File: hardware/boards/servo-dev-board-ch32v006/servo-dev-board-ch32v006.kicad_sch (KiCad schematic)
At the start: 0 parts

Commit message: copy pasted sg90 prd ch32v006 schematics, and modify to fit. PCB should be about 85x65mm to accomodate TP ring rails for easy hardware testing.
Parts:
- added C1, C8: 10µF, Capacitor_SMD:C_0603_1608Metric, symbol Device:C
- added C2, C3: 1µF, Capacitor_SMD:C_0402_1005Metric, symbol Device:C
- added C4, C5, C6, C7, C9: 0.1µF, Capacitor_SMD:C_0402_1005Metric, symbol Device:C
- added D1: ESD, Diode_SMD:D_SOD-882, symbol Diode:PESD5V0L1UL
- added FB1: 600Ω@100MHz, Inductor_SMD:L_0603_1608Metric, symbol Device:FerriteBead_Small
- added J1: Servo Input, shared:Servo_Output_Pads, symbol Connector_Generic:Conn_01x03
- added J2: Motor, shared:Motor_Wire_Pads, symbol Connector_Generic:Conn_01x02
- added J3: Debug, shared:Debug_Pads_1x4_P1.27mm, symbol Connector_Generic:Conn_01x04
- added J4: Potentiometer, shared:Pot_Wire_Pads, symbol Connector_Generic:Conn_01x03
- added NT2: NetTie_2, shared:NetTie-2_SMD_0.2mm, symbol Device:NetTie_2
- added Q1: AO3401A, Package_TO_SOT_SMD:SOT-23, symbol Transistor_FET:AO3401A
- added R1: 47kΩ, Resistor_SMD:R_0402_1005Metric, symbol Device:R
- added R10, R12, R3, R5, R6: 10kΩ, Resistor_SMD:R_0402_1005Metric, symbol Device:R
- added R11, R9: 20kΩ, Resistor_SMD:R_0402_1005Metric, symbol Device:R
- added R13: 68Ω, Resistor_SMD:R_0402_1005Metric, symbol Device:R
- added R2: 4.7kΩ, Resistor_SMD:R_0402_1005Metric, symbol Device:R
- added R4: 0.1Ω 1%, Resistor_SMD:R_1206_3216Metric, symbol Device:R
- added TH1: NTC 10k, Resistor_SMD:R_0402_1005Metric, symbol Device:Thermistor
- added TP1: TestPoint_Probe, TestPoint:TestPoint_Keystone_5015_Micro_Mini, symbol Connector:TestPoint_Probe
- added U1: TPAP2210K-3.3TRG1, shared:SOT-23-5_L2.9-W1.6-P0.95-LS2.8-BR, symbol shared:TPAP2210K-3.3TRG1
- added U2: 74LVC2G125RA3-7, shared:X2-DFN1210-8_L1.2-W1.0-P0.30-BL, symbol shared:74LVC2G125RA3-7
- added U3: DRV8837DSGR-JSM, Package_SON:WSON-8-1EP_2x2mm_P0.5mm_EP0.9x1.6mm, symbol Driver_Motor:DRV8837C
- added U4: CH32V006F8U6, shared:UQFN-20_L3.0-W3.0-P0.40-BL-EP1.7, symbol shared:CH32V006F8U6
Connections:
- new net +3.3V: C3.1, C4.1, C9.1, FB1.1, J3.1 (Pin_1), J4.1 (Pin_1), R1.2, R5.1, R6.1, U1.5 (VOUT), U2.8 (VCC), U4.6 (VDD)
- new net 3V3_DRV: C6.1, FB1.2, U3.8 (VCC)
- new net BUF: R13.1, U2.5 (2A), U2.6 (1Y)
- new net DATA: D1.1 (K), J1.3 (Pin_3), R13.2
- new net DBG: TP1.1, U4.9 (PC2/T1C3N_/T2/SCL)
- new net DE: U2.7 (~{2OE}), U4.5 (PD0/T1/TX_/SDA_/OPN1)
- new net EN: R3.1, U3.7 (~{SLEEP}), U4.12 (PC5/T1C2_/T1/T2/TX_/SCK)
- new net ENC_A: U4.19 (PD5/T2/TX/RX_/MISO_/A5)
- new net ENC_B: U4.20 (PD6/T2/RX/TX_/MOSI_/A6)
- new net GND: C1.2, C2.2, C3.2, C4.2, C5.2, C9.2, D1.2 (A), J1.1 (Pin_1), J3.2 (Pin_2), J4.3 (Pin_3), Q1.1 (G), R10.2, R12.2, R4.1, TH1.2, U1.2 (GND), U2.2 (1A), U2.4 (GND), U4.21 (VSS), U4.4 (VSS)
- new net IN1: U3.6 (IN1), U4.13 (PC6/T1C3_/T1/RX_/MOSI)
- new net IN2: U3.5 (IN2), U4.14 (PC7/T1C4_/T1/T2/MISO)
- new net ISNS: NT2.1
- new net ISNS+: U4.3 (PA2/T1/T2/U2TX_/OPP0/XO/A0)
- new net ISNS-: U4.2 (PA1/T1/T2/OPN0/XI/A1)
- new net LED: U4.10 (PC3/T1/T2)
- new net OUTA: J2.1 (Pin_1), R9.1, U3.2 (OUT1)
- new net OUTB: J2.2 (Pin_2), R11.1, U3.3 (OUT2)
- new net PGND: C6.2, C7.2, C8.2, NT2.2, R3.2, R4.2, U3.4 (GND), U3.9 (GND)
- new net POT: J4.2 (Pin_2), R2.1
- new net RX: U2.3 (2Y), U4.8 (PC1/T1C2N_/T2/RX_/SDA/NSS)
- new net SWDIO: J3.3 (Pin_3), U4.15 (PD1/SWIO/T1/SCL_/RX_/OPP3)
- new net TX: R1.1, U2.1 (~{1OE}), U4.7 (PC0/T1C1N_/T1/T2/TX_/MOSI_)
- new net VIN: J1.2 (Pin_2), Q1.2 (S)
- new net VNTC: R5.2, TH1.1, U4.18 (PD4/T1/T2/SCK_/OPO0/A7)
- new net VPOS: C5.1, R2.2, U4.16 (PD2/T1/T2/U2TX_/A3)
- new net VSNA: R10.1, R9.2, U4.11 (PC4/T1C1_/T1/MCO/A2)
- new net VSNB: R11.2, R12.1, U4.17 (PD3/T1/T2/U2RX_/NSS_/OPP2/A4)
- new net VSYS: C1.1, C2.1, C7.1, C8.1, Q1.3 (D), U1.1 (VIN), U1.3 (EN), U3.1 (VM)
- new net nRST: J3.4 (Pin_4), R6.2, U4.1 (PD7/RST/T2C4/OPP1/PA4/U2TX_/OPN2)
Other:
- note added: "BEMF SENSE"
- note added: "COMMUNICATION"
- note added: "CONNECTORS"
- note added: "CURRENT SENSE"
- note added: "MCU"
- note added: "MOTOR DRIVER"
- note added: "POSITION SENSOR FILTERING"
- note added: "POWER"
- note added: "TEMP SENSE"

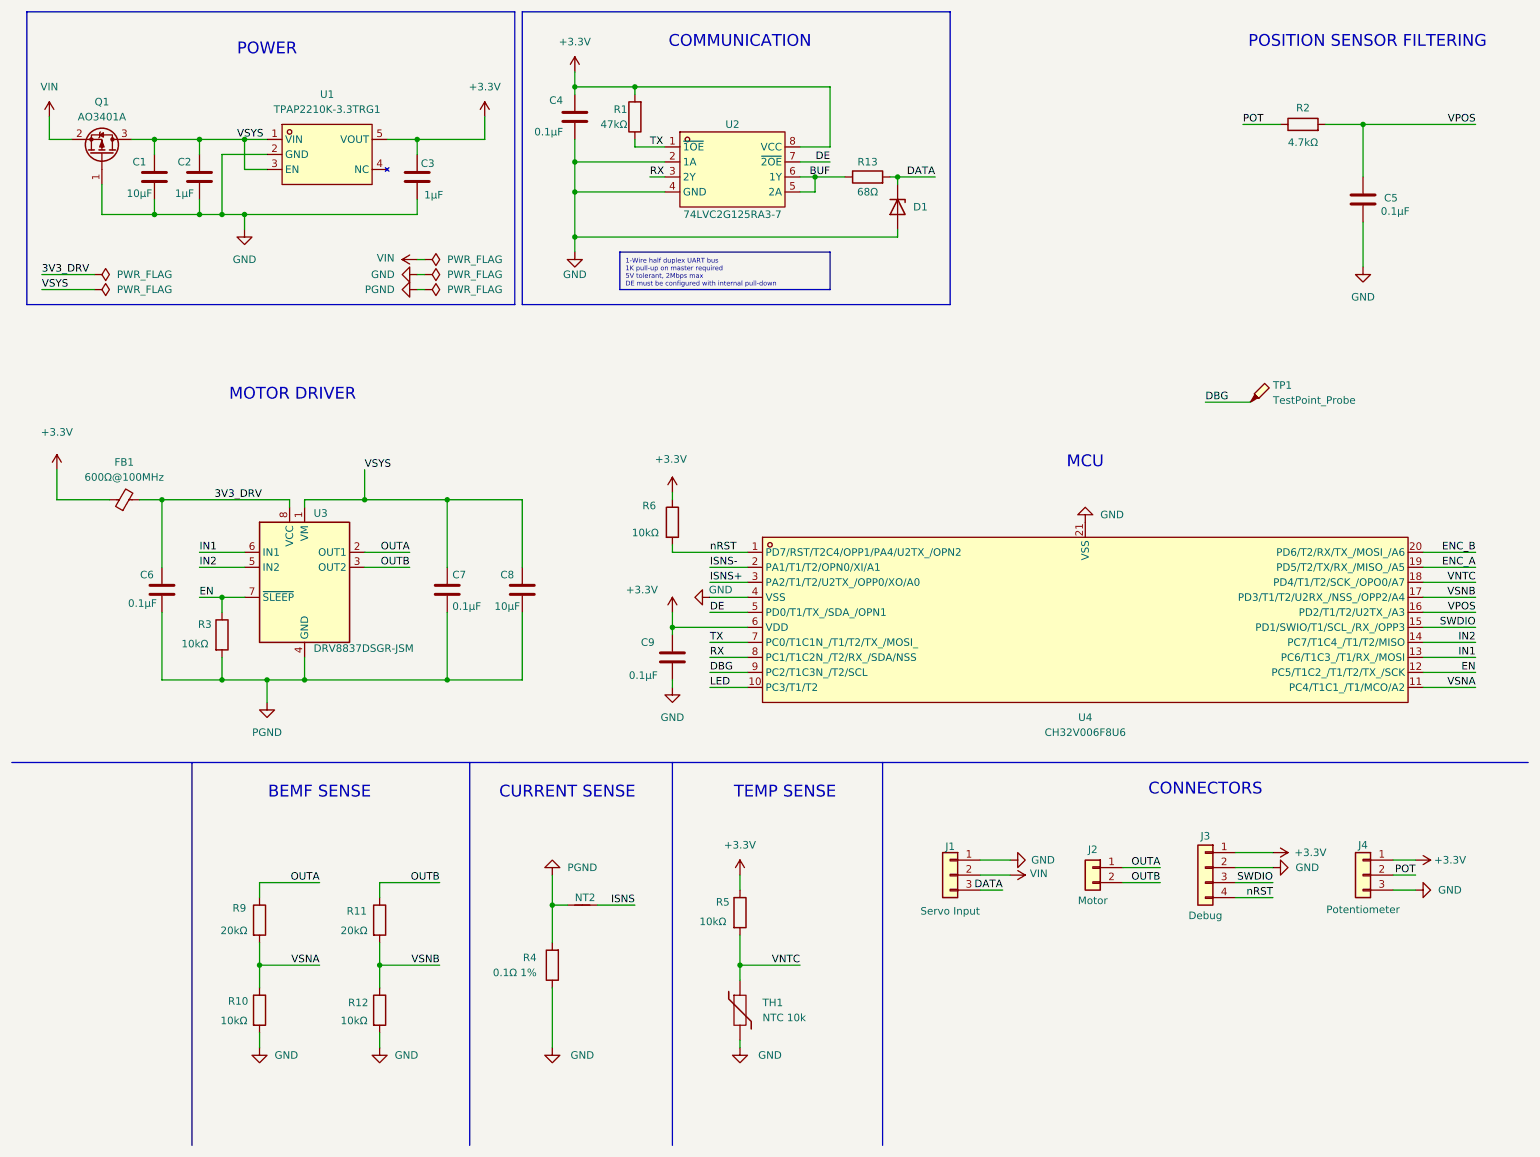
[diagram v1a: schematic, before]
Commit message: mostly done with ch32v006 based dev board schematics. Next is to pick footprint / parts and proceed to PCB design
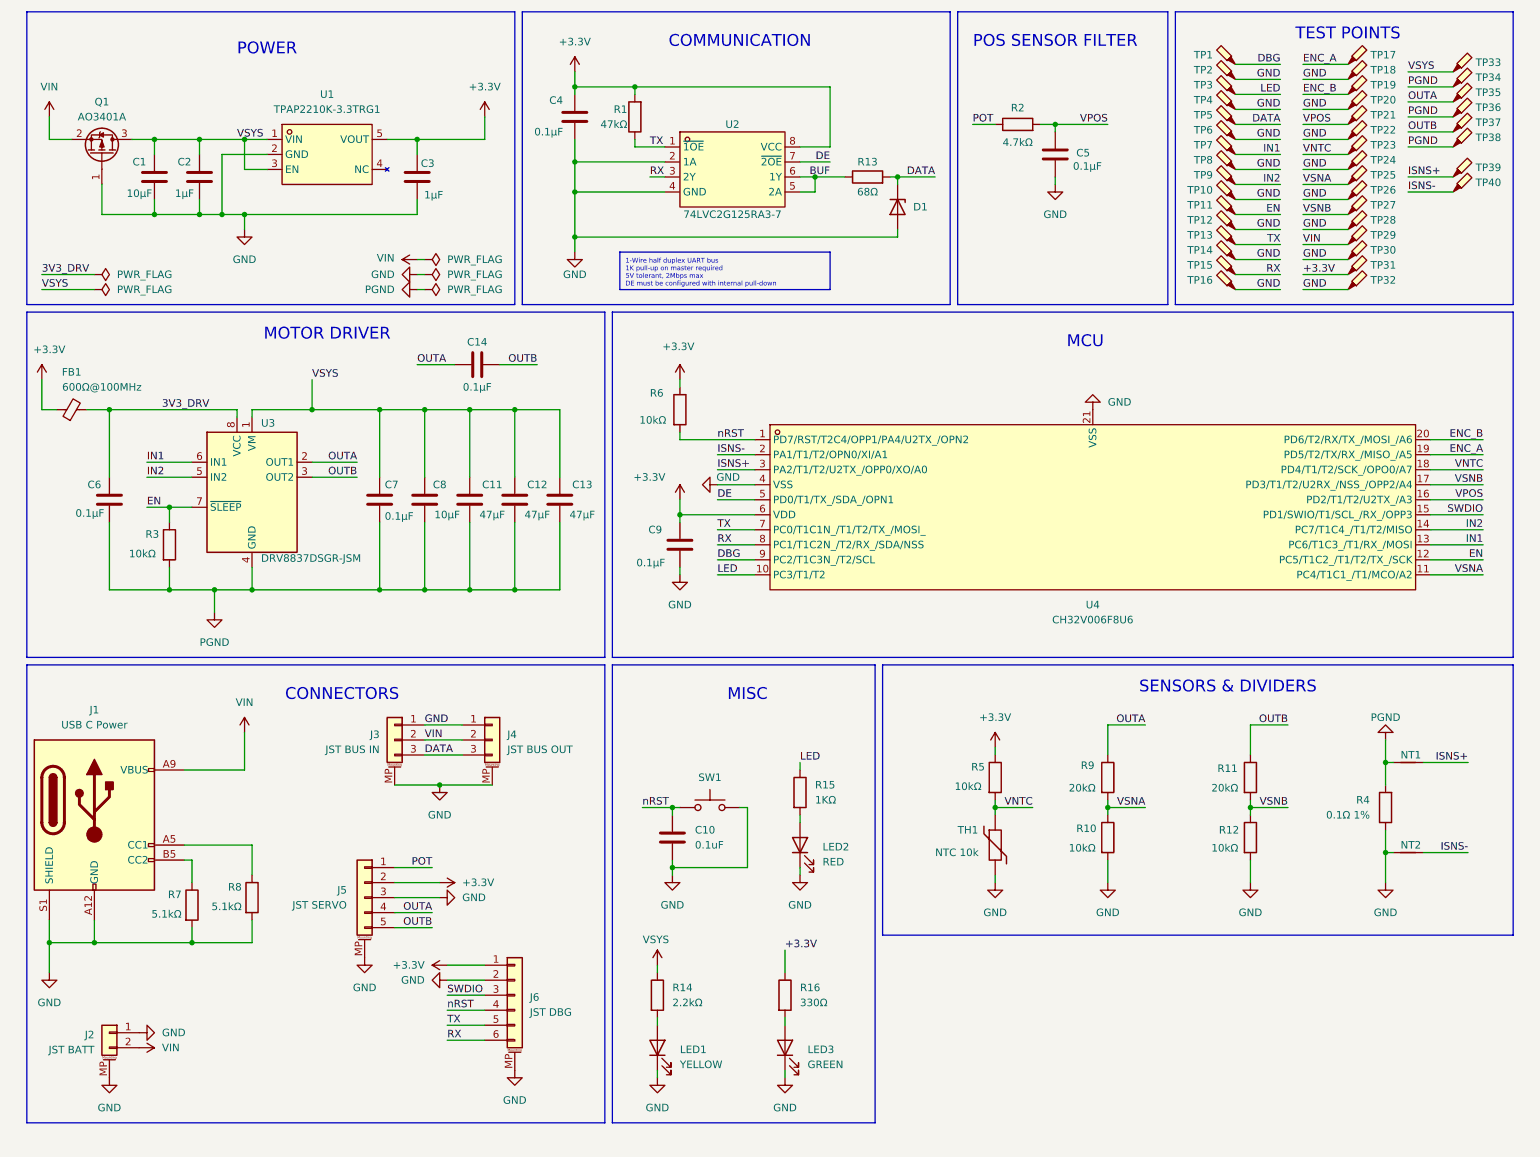
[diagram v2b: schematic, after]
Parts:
- removed J1: Servo Input, shared:Servo_Output_Pads, symbol Connector_Generic:Conn_01x03
- removed J2: Motor, shared:Motor_Wire_Pads, symbol Connector_Generic:Conn_01x02
- removed J3: Debug, shared:Debug_Pads_1x4_P1.27mm, symbol Connector_Generic:Conn_01x04
- removed J4: Potentiometer, shared:Pot_Wire_Pads, symbol Connector_Generic:Conn_01x03
- added C10: 0.1uF, Capacitor_SMD:C_0402_1005Metric, symbol Device:C
- added C11, C12, C13: 47µF, Capacitor_SMD:C_1206_3216Metric, symbol Device:C
- added C14: 0.1µF, Capacitor_SMD:C_0402_1005Metric, symbol Device:C
- added J1: USB C Power, symbol Connector:USB_C_Receptacle_PowerOnly_6P
- added J2: JST BATT, symbol Connector_Generic_MountingPin:Conn_01x02_MountingPin
- added J3: JST BUS IN, symbol Connector_Generic_MountingPin:Conn_01x03_MountingPin
- added J4: JST BUS OUT, symbol Connector_Generic_MountingPin:Conn_01x03_MountingPin
- added J5: JST SERVO, symbol Connector_Generic_MountingPin:Conn_01x05_MountingPin
- added J6: JST DBG, symbol Connector_Generic_MountingPin:Conn_01x06_MountingPin
- added LED1: YELLOW, LED_SMD:LED_0805_2012Metric, symbol Device:LED
- added LED2: RED, LED_SMD:LED_0805_2012Metric, symbol Device:LED
- added LED3: GREEN, LED_SMD:LED_0805_2012Metric, symbol Device:LED
- added NT2: NetTie_2, shared:NetTie-2_SMD_0.2mm, symbol Device:NetTie_2
- added R14: 2.2kΩ, Resistor_SMD:R_0402_1005Metric, symbol Device:R
- added R15: 1KΩ, Resistor_SMD:R_0402_1005Metric, symbol Device:R
- added R16: 330Ω, Resistor_SMD:R_0402_1005Metric, symbol Device:R
- added R7, R8: 5.1kΩ, Resistor_SMD:R_0402_1005Metric, symbol Device:R
- added SW1: SW_Push, Button_Switch_SMD:SW_SPST_PTS810, symbol Switch:SW_Push
- added TP10, TP11, TP12, TP13, TP14, TP15, TP16, TP17, TP18, TP19, TP2, TP20, TP21, TP22, TP23, TP24, TP25, TP26, TP27, TP28, TP29, TP3, TP30, TP31, TP32, TP33, TP34, TP35, TP36, TP37, TP38, TP39, TP4, TP40, TP5, TP6, TP7, TP8, TP9: TestPoint_Probe, TestPoint:TestPoint_Keystone_5015_Micro_Mini, symbol Connector:TestPoint_Probe
- renumbered NT2 to NT1
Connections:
- net ISNS is gone; now on net ISNS+: NT1.1
- net +3.3V: now also J5.2 (Pin_2), J6.1 (Pin_1), R16.1, TP31.1
- net DATA: now also J3.3 (Pin_3), J4.3 (Pin_3), TP5.1
- net EN: now also TP11.1
- net ENC_A: now also TP17.1
- net ENC_B: now also TP19.1
- net GND: now also C10.1, J1.A12 (GND), J1.B12 (GND), J1.S1 (SHIELD), J2.1 (Pin_1), J2.MP (MountPin), J3.1 (Pin_1), J3.MP (MountPin), J4.1 (Pin_1), J4.MP (MountPin), J5.3 (Pin_3), J5.MP (MountPin), J6.2 (Pin_2), J6.MP (MountPin), LED1.1 (K), LED2.1 (K), LED3.1 (K), NT2.2, R7.2, R8.2, SW1.2, TP10.1, TP12.1, TP14.1, TP16.1, TP18.1, TP2.1, TP20.1, TP22.1, TP24.1, TP26.1, TP28.1, TP30.1, TP32.1, TP4.1, TP6.1, TP8.1
- net IN1: now also TP7.1
- net IN2: now also TP9.1
- net ISNS+: now also TP39.1
- net ISNS-: now also NT2.1, TP40.1
- net LED: now also R15.1, TP3.1
- net OUTA: now also C14.1, J5.4 (Pin_4), TP35.1
- net OUTB: now also C14.2, J5.5 (Pin_5), TP37.1
- net PGND: now also C11.2, C12.2, C13.2, TP34.1, TP36.1, TP38.1
- net POT: now also J5.1 (Pin_1)
- net RX: now also J6.6 (Pin_6), TP15.1
- net SWDIO: now also J6.3 (Pin_3)
- net TX: now also J6.5 (Pin_5), TP13.1
- net VIN: now also J1.A9 (VBUS), J1.B9 (VBUS), J2.2 (Pin_2), J3.2 (Pin_2), J4.2 (Pin_2), TP29.1
- net VNTC: now also TP23.1
- net VPOS: now also TP21.1
- net VSNA: now also TP25.1
- net VSNB: now also TP27.1
- net VSYS: now also C11.1, C12.1, C13.1, R14.1, TP33.1
- net nRST: now also C10.2, J6.4 (Pin_4), SW1.1
- new net: LED1.2 (A), R14.2
- new net: LED2.2 (A), R15.2
- new net: J1.A5 (CC1), R8.1
- new net: J1.B5 (CC2), R7.1
- new net: LED3.2 (A), R16.2
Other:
- note added: "MISC"
- note added: "POS SENSOR FILTER"
- note added: "SENSORS & DIVIDERS"
- note added: "TEST POINTS"
- note removed: "BEMF SENSE"
- note removed: "CURRENT SENSE"
- note removed: "POSITION SENSOR FILTERING"
- note removed: "TEMP SENSE"
- moved on the sheet: C5, C6, C7, C8, C9, FB1, NT1, R10, R11, R12, R2, R3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

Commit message: wip
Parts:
- removed J1: USB C Power, symbol Connector:USB_C_Receptacle_PowerOnly_6P
- removed TP11, TP12, TP13, TP14, TP15, TP16, TP27, TP28, TP29, TP30, TP31, TP32, TP38: TestPoint_Probe, TestPoint:TestPoint_Keystone_5015_Micro_Mini, symbol Connector:TestPoint_Probe
- added H1, H2, H3, H4: MountingHole_Pad_MP, MountingHole:MountingHole_2.2mm_M2_ISO7380_Pad, symbol Mechanical:MountingHole_Pad
- added J5: JST ENC, Connector_JST:JST_ZH_S4B-ZR-SM4A-TF_1x04-1MP_P1.50mm_Horizontal, symbol Connector_Generic_MountingPin:Conn_01x04_MountingPin
- added USB1: TYPE-C 6P(073), shared:TYPE-C-SMD_TYPE-C-6P-073, symbol shared:TYPE-C6P(073)
- J1: renamed from J2; footprint (none) -> Connector_JST:JST_PH_S2B-PH-SM4-TB_1x02-1MP_P2.00mm_Horizontal
- J2: renamed from J3; footprint (none) -> Connector_JST:JST_ZH_B3B-ZR-SM4-TF_1x03-1MP_P1.50mm_Vertical
- J3: renamed from J4; footprint (none) -> Connector_JST:JST_ZH_B3B-ZR-SM4-TF_1x03-1MP_P1.50mm_Vertical
- J4: renamed from J5; footprint (none) -> Connector_JST:JST_ZH_S5B-ZR-SM4A-TF_1x05-1MP_P1.50mm_Horizontal
- J6: footprint (none) -> Connector_JST:JST_ZH_S6B-ZR-SM4A-TF_1x06-1MP_P1.50mm_Horizontal
- renumbered C14 to C10, C12 to C11, C13 to C12, C9 to C13, C10 to C14, C11 to C9, LED3 to LED2, LED2 to LED3, R15 to R10, R5 to R11, R9 to R12, R10 to R13, R11 to R14, R12 to R15, R13 to R2, R2 to R3, R3 to R4, R6 to R5, R7 to R6, R8 to R7, R14 to R8, R16 to R9, R4 to RS1, TP17 to TP11, TP18 to TP12, TP19 to TP13, TP20 to TP14, TP21 to TP15, TP22 to TP16, TP23 to TP17, TP24 to TP18, TP25 to TP19, TP26 to TP20, TP33 to TP21, TP34 to TP22, TP35 to TP23, TP36 to TP24, TP37 to TP25, TP39 to TP26, TP40 to TP27
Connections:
- net +3.3V: now also TP13.1, J5.1 (Pin_1)
- net DATA: now also TP4.1; no longer TP5.1
- net DBG: now also TP2.1; no longer TP1.1
- net EN: now also TP7.1
- net GND: now also R6.1, R7.1, TP1.1, TP11.1, H1.1, H2.1, H3.1, H4.1, J5.2 (Pin_2), J5.MP (MountPin), USB1.7 (EH), USB1.A12 (GND), USB1.B12 (GND); no longer R6.2, R7.2, TP12.1, TP14.1, TP16.1, TP18.1, TP2.1, TP4.1, TP6.1, TP8.1
- net IN1: now also TP5.1; no longer TP7.1
- net IN2: now also TP6.1; no longer TP9.1
- net OUTB: now also TP24.1; no longer TP25.1
- net PGND: now also TP21.1, TP25.1; no longer TP22.1, TP24.1
- net RX: now also TP9.1
- net TX: now also TP8.1
- net VIN: now also TP12.1, USB1.A9 (VBUS), USB1.B9 (VBUS)
- net VNTC: now also TP15.1; no longer TP17.1
- net VPOS: now also TP14.1; no longer TP15.1
- net VSNA: now also TP16.1; no longer TP19.1
- net VSNB: now also TP17.1
- net VSYS: now also TP22.1; no longer TP21.1
- net ENC_A renamed ENCA
- net ENCA: now also TP18.1, J5.3 (Pin_3); no longer TP11.1
- net ENC_B renamed ENCB
- net ENCB: now also TP19.1, J5.4 (Pin_4); no longer TP13.1
- new net: R6.2, USB1.A5 (CC1)
- new net: R7.2, USB1.B5 (CC2)
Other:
- note added: "TEST POINTS / MOUNTING HOLES"
- note removed: "TEST POINTS"
- moved on the sheet: J1, J2, J3, J4, J6, R6, R7, TP1, TP10, TP11, TP12, TP13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

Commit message: completed board design
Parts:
- removed TP21: TestPoint_Probe, TestPoint:TestPoint_Keystone_5015_Micro_Mini, symbol Connector:TestPoint_Probe
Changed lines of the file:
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@@
 	(wire
 		(pts
-			(xy 255.27 26.67) (xy 247.65 26.67)
-		)
-		(stroke
-			(width 0)
-			(type default)
-		)
-	)
-	(wire
-		(pts
 			(xy 196.85 161.29) (xy 196.85 157.48)
 		)
@@
 		)
 	)
-	(label "PGND"
-		(at 247.65 26.67 0)
-		(effects
-			(font
-				(size 1.27 1.27)
-			)
-			(justify left bottom)
-		)
-	)
 	(label "TX"
 		(at 226.06 43.18 180)
@@
 					(unit 1)
 				)
-			)
-		)
-	)
-	(symbol
-		(lib_id "Connector:TestPoint_Probe")
-		(at 255.27 26.67 0)
-		(unit 1)
-		(exclude_from_sim no)
-		(in_bom yes)
-		(on_board yes)
-		(dnp no)
-		(fields_autoplaced yes)
-		(property "Reference" "TP21"
-			(at 259.08 25.0824 0)
-			(effects
-				(font
-					(size 1.27 1.27)
-				)
-				(justify left)
-			)
-		)
-		(property "Value" "TestPoint_Probe"
-			(at 259.08 26.3524 0)
-			(effects
-				(font
-					(size 1.27 1.27)
-				)
-				(justify left)
-				(hide yes)
-			)
-		)
-		(property "Footprint" "TestPoint:TestPoint_Keystone_5015_Micro_Mini"
-			(at 260.35 26.67 0)
-			(effects
-				(font
-					(size 1.27 1.27)
-				)
-				(hide yes)
-			)
-		)
-		(property "Datasheet" "~"
-			(at 260.35 26.67 0)
-			(effects
-				(font
-					(size 1.27 1.27)
-				)
-				(hide yes)
-			)
-		)
-		(property "Description" "test point (alternative probe-style design)"
-			(at 255.27 26.67 0)
-			(effects
-				(font
-					(size 1.27 1.27)
-				)
-				(hide yes)
-			)
-		)
-		(pin "1"
-		)
-		(instances
-			(project "servo-dev-board-ch32v006"
-				(path "/6062e7d2-0c72-467e-b49c-6387ba053e09"
-					(reference "TP21")
-					(unit 1)
-				)

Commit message: addressing review issues
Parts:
- removed J1: JST BATT, Connector_JST:JST_PH_S2B-PH-SM4-TB_1x02-1MP_P2.00mm_Horizontal, symbol Connector_Generic_MountingPin:Conn_01x02_MountingPin
- added C14: 10µF, Capacitor_SMD:C_0603_1608Metric, symbol Device:C
- added J1: BATT JST-PH, shared:CONN-TH_S2B-PH-K-S-LF-SN, symbol shared:S2B-PH-K-S(LF)(SN)
- added Q1, Q3: AO3401A, Package_TO_SOT_SMD:SOT-23, symbol Transistor_FET:AO3401A
- added R1, R2, R3: 100kΩ, Resistor_SMD:R_0402_1005Metric, symbol Device:R
- J2: value JST BUS IN -> BUS JST-ZH
- J3: value JST BUS OUT -> BUS JST-ZH
- J4: value JST SERVO -> SERVO JST-ZH
- J5: value JST ENC -> ENC JST-ZH
- J6: value JST DBG -> DBG JST-ZH
- TP1: LCSC (none) -> C5199798
- renumbered C9 to C10, C14 to C13, C13 to C15, C10 to C7, C7 to C8, C8 to C9, Q1 to Q2, R7 to R10, R8 to R11, R9 to R12, R10 to R13, R11 to R14, R12 to R15, R13 to R16, R14 to R17, R15 to R18, R1 to R4, R2 to R5, R3 to R6, R4 to R7, R5 to R8, R6 to R9, TP22 to TP21, TP23 to TP22, TP24 to TP23, TP25 to TP24, TP26 to TP25, TP27 to TP26
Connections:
- net +3.3V: now also C14.1
- net GND: now also C14.2, J1.1; no longer Q2.1 (G)
- net ISNS+: now also TP26.1; no longer TP25.1
- net ISNS-: now also TP25.1; no longer TP26.1
- net POT: now also R6.2; no longer R6.1
- net VPOS: now also R6.1; no longer R6.2
- net VSYS: now also Q1.3 (D), Q3.3 (D), R1.2, R2.2, R3.2
- net VIN renamed BUS_VIN
- net BUS_VIN: now also Q3.2 (S); no longer Q2.2 (S), USB1.A9 (VBUS), USB1.B9 (VBUS)
- new net: Q2.1 (G), R2.1
- new net: Q1.1 (G), R1.1
- new net: Q3.1 (G), R3.1
- new net VBAT: J1.2, Q2.2 (S)
- new net VBUS: Q1.2 (S), USB1.A9 (VBUS), USB1.B9 (VBUS)
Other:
- note added: "FILTER"
- note added: "LED"
- note added: "MICROCONTROLLER"
- note added: "Mounting Holes"
- note added: "POWER FLAGS"
- note added: "POWER INPUT"
- note added: "POWER REGULATION"
- note added: "RESET SWITCH"
- note added: "TEST POINTS"
- note removed: "MCU"
- note removed: "MISC"
- note removed: "POS SENSOR FILTER"
- note removed: "POWER"
- note removed: "TEST POINTS / MOUNTING HOLES"
- moved on the sheet: C1, C13, C15, C2, C3, C4, C5, C7, D1, H1, H2, H3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
